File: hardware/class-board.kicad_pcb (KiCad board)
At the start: 4 copper layers, 180 x 100 mm, 334 parts, among them J1 DevKit J1 (left row), J10 C2937625_-_Conn_01x03, J11 C2937625_-_Conn_01x03, J12 C2937625_-_Conn_01x03, J13 C492401-PZ254V-11-02P, J2 DevKit J3 (right row), J201 USB-C 16P, J202 DC005-T20, J3 C2937625_-_Conn_01x03, J4 Qwiic, J5 Expansion 2x10, J6 Panel link 2x20 female, J7 Panel link 2x20 female, J8 Panel link 2x20 female, J9 C2937625_-_Conn_01x03, J901 KF301-5.0-2P, J903 KF301-5.0-2P, J905 KF301-5.0-3P, Q901 AOD4185, Q904 AOD4184A, U101 ADS8688IDBTR, U201 LM66100DCKR, U202 LM66100DCKR, U203 78L05G-AB3-R, U204 AMS1117-3.3, U301 DAC8563SDGSR, U302 74HCT125PW, U303 OPA2192IDR, U501 SN74AHCT541PWR, U502 74HCT125PW, U503 SN74LVC1T45DBVR, U505 TCA9535PWR, U701 SI5351A-B-GT, U702 74HC74D,653, U703 OPA1656IDR, U704 DG419DY-T1-E3, U705 OPA1612AIDR, U706 OPA1612AIDR, U801 AD9834BRUZ, U802 OPA564AIDWPR, U901 TS5A23157DGSR, U902 TS5A23157DGSR, U903 DRV8871DDAR, U904 UCC27517DBVR, Y701 25 MHz

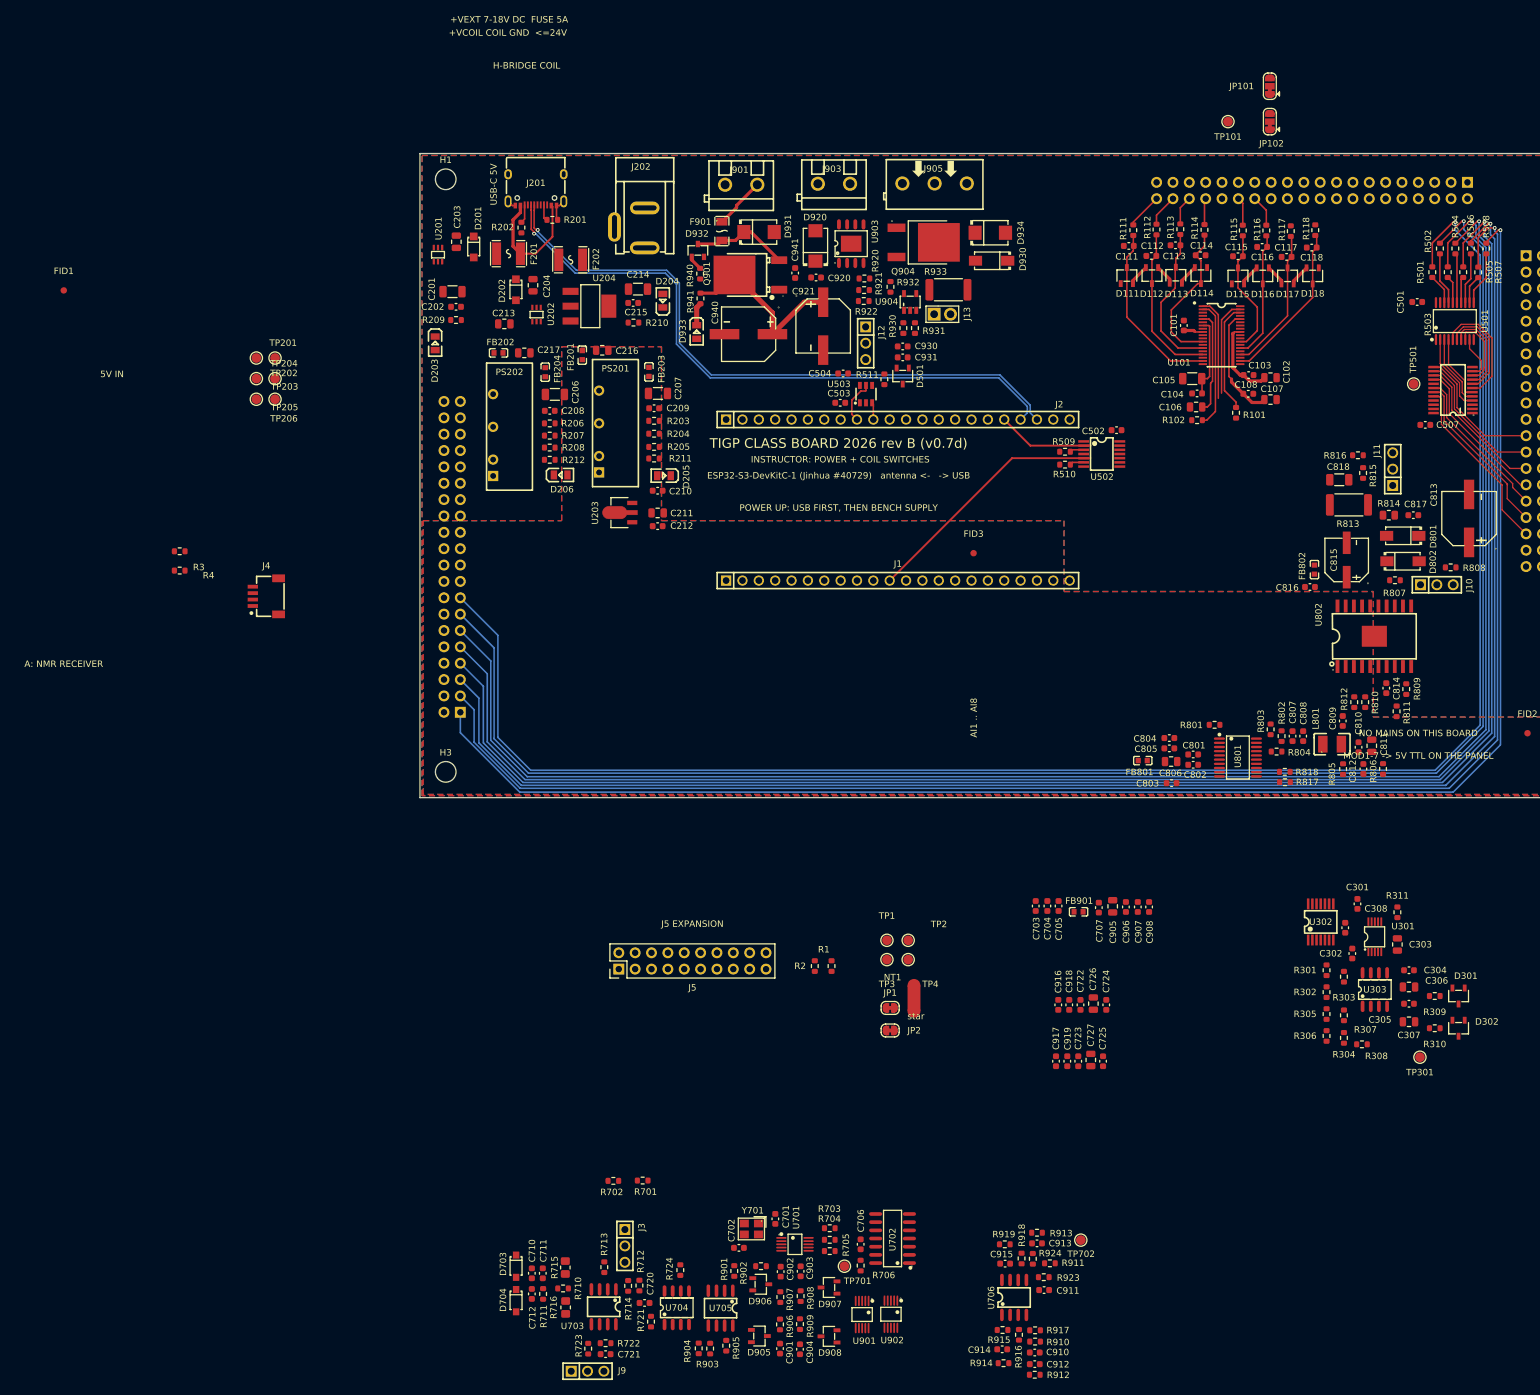
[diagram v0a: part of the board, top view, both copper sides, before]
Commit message: hardware: main-board PCB from the instructor's 2026-09-19 05:05 save (790 tracks, 17 parts still parked)
Co-Authored-By: Claude Fable 5.1 <noreply@anthropic.com>
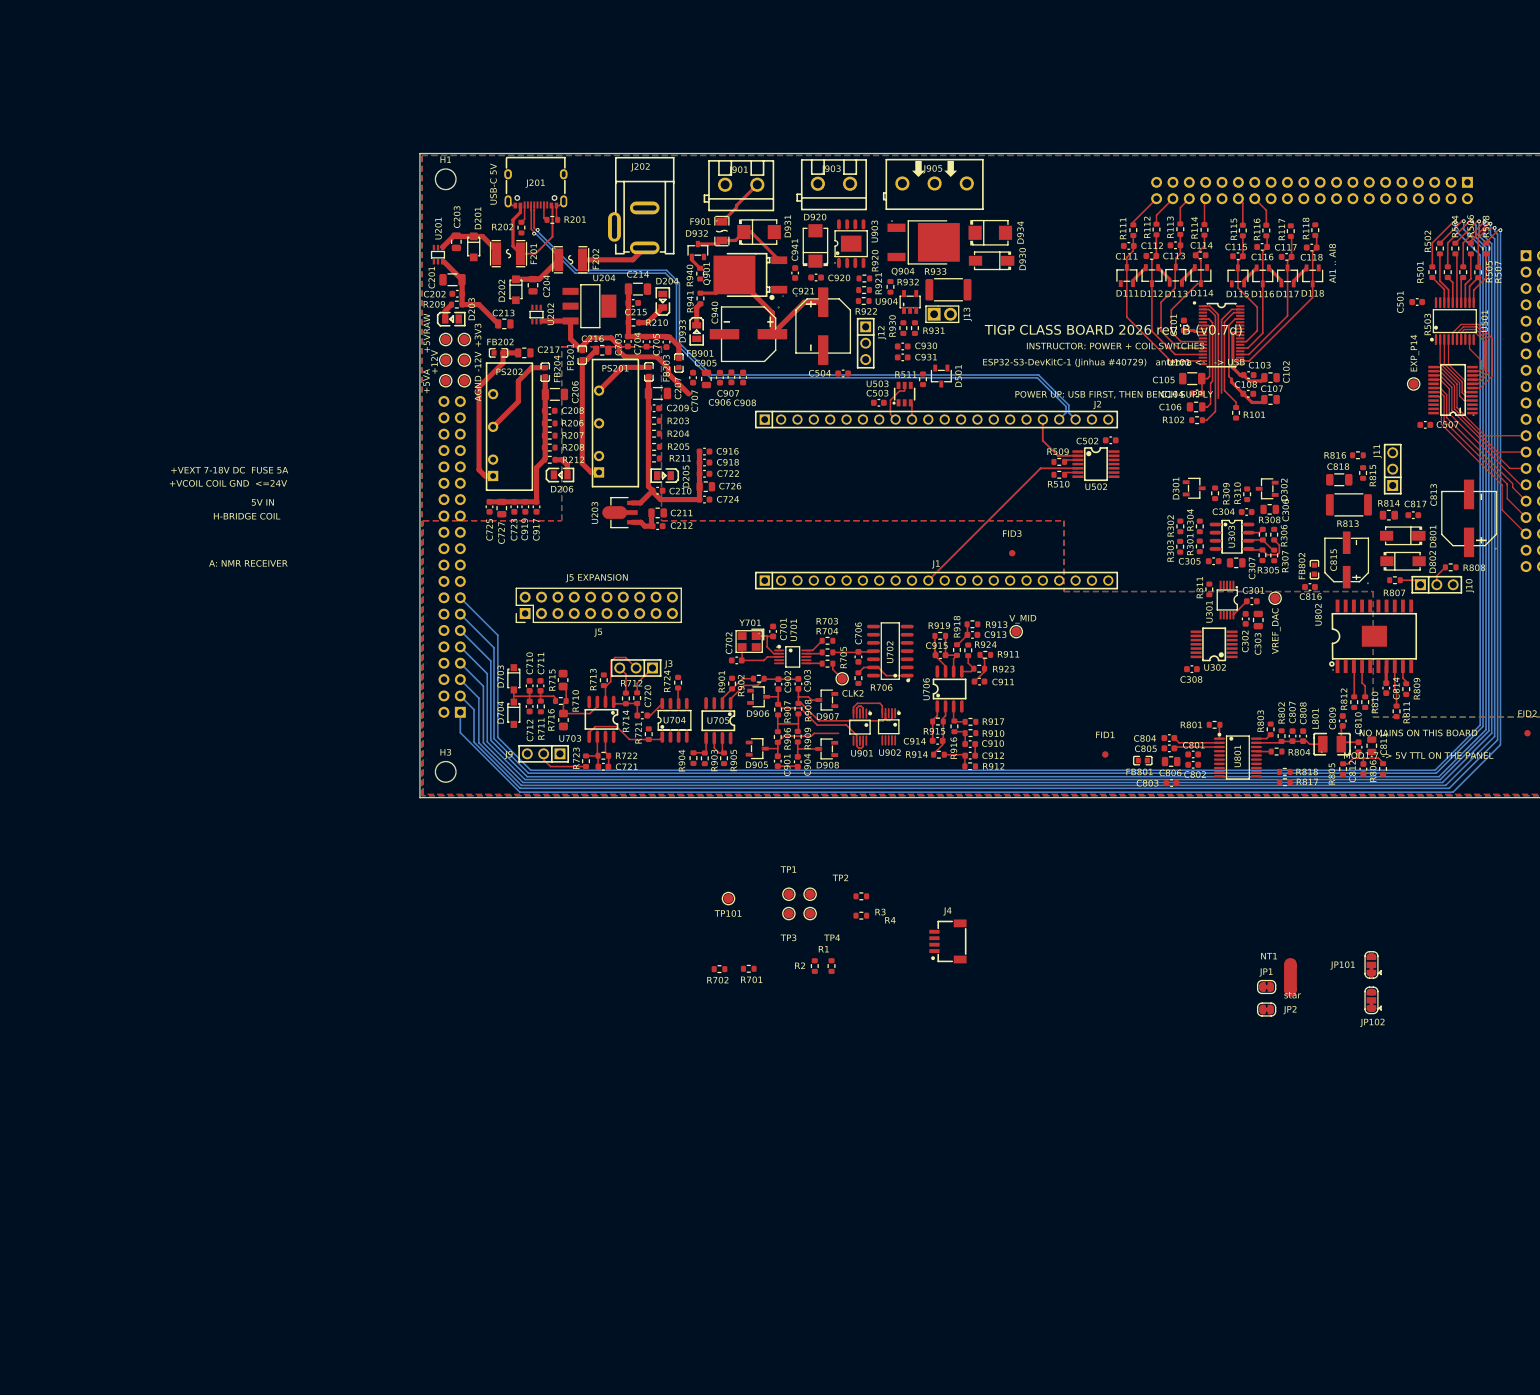
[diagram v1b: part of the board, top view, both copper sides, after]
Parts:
- moved FID1 177.0 mm to (106.4, 108.3)
- moved TP101 143.4 mm to (47.9, 130.7)
- moved JP101 137.3 mm to (147.7, 141.0)
- moved JP102 137.3 mm to (147.7, 146.5)
- moved C725 128.4 mm to (10.8, 69.8), turned to -90 degrees
- moved C727 125.3 mm to (12.7, 70.1), turned to -90 degrees
- moved C723 122.8 mm to (14.7, 69.8), turned to -90 degrees
- moved C919 120.4 mm to (16.4, 69.8), turned to -90 degrees
- moved J4 118.6 mm to (81.9, 137.3)
- moved R3 118.6 mm to (68.5, 130.3)
- moved R4 118.6 mm to (68.5, 133.3)
- moved C917 118.0 mm to (18.1, 69.8), turned to -90 degrees
- moved C703 108.1 mm to (32.3, 44.2)
- moved C704 107.5 mm to (35.2, 44.2), turned to -90 degrees
- moved C705 106.6 mm to (38.3, 44.3), turned to -90 degrees
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- renumbered TP203 to +12V, TP202 to +3V3, TP205 to +5VA, TP201 to +5VRAW, TP204 to -12V, TP206 to AGND, TP701 to CLK2, TP501 to EXP_P14, TP301 to VREF_DAC, TP702 to V_MID
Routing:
- net +5V_RAW: track 0.00 -> 46.8 mm
- net +12V: track 13.2 -> 50.5 mm
- net -12V: track 6.46 -> 33.7 mm
- net Net-(PS202-+VIN): track 0.00 -> 24.6 mm
- net /nmr_rx/SN_B: track 0.00 -> 23.3 mm
- net /nmr_rx/SN_A: track 0.00 -> 22.2 mm
- net Net-(PS201-+VIN): track 0.00 -> 22.1 mm
- net +3V3: track 17.8 -> 38.2 mm
- net /nmr_rx/SP_A: track 0.00 -> 17.0 mm
- net Net-(PS202--VO): track 0.00 -> 13.8 mm
- net /nmr_rx/ST2_IN: track 0.00 -> 13.4 mm
- net /nmr_rx/S_MINUS: track 0.00 -> 12.5 mm
- net /b1_inputs/AUX: track 0.00 -> 12.2 mm
- net /nmr_rx/LNA_FB1: track 0.00 -> 11.9 mm
- net /nmr_rx/RX_IN: track 0.00 -> 11.0 mm
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
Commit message: WIP main board routing + schematic (instructor), 2026-09-21 05:04
Co-Authored-By: Claude Fable 5.1 <noreply@anthropic.com>
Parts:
- removed +12V, +3V3, +5VA, +5VRAW, -12V, AGND, EXP_P14, VREF_DAC: TP, class_board:TestPoint_Pad_D1.5mm
- removed CLK2: CLK2, class_board:TestPoint_Pad_D1.5mm
- removed JP1, JP2: SolderJumper_2_Bridged, class_board:SolderJumper-2_P1.3mm_Bridged_RoundedPad1.0x1.5mm
- removed JP101, JP102: SolderJumper_3_Bridged12, class_board:SolderJumper-3_P1.3mm_Bridged12_RoundedPad1.0x1.5mm
- removed NT1: AGND-GND star, class_board:NetTie-2_SMD_Pad2.0mm
- removed V_MID: V_MID, class_board:TestPoint_Pad_D1.5mm
- added J14: C2937625_-_Conn_01x03, DDS_Library:C2937625-HDR-TH_3P-P2.54-V-M, F.Cu at (136.9, 31.3)
- added J15: C2937625_-_Conn_01x03, DDS_Library:C2937625-HDR-TH_3P-P2.54-V-M, F.Cu at (138.6, 28.0)
- added R717: 0, Resistor_SMD:R_0805_2012Metric_Pad1.20x1.40mm_HandSolder, F.Cu at (11.4, 76.9)
- added R718: 0, Resistor_SMD:R_0805_2012Metric_Pad1.20x1.40mm_HandSolder, F.Cu at (11.3, 79.1)
- added R719: 0, Resistor_SMD:R_0805_2012Metric_Pad1.20x1.40mm_HandSolder, F.Cu at (113.4, 142.4)
- added TP201: 5V_RAW, class_board:TestPoint_Pad_D1.5mm, F.Cu at (8.80, 33.7)
- added TP202: +3V3, class_board:TestPoint_Pad_D1.5mm, F.Cu at (20.8, 36.8)
- added TP203: +12V, class_board:TestPoint_Pad_D1.5mm, F.Cu at (44.1, 56.5)
- added TP204: -12V, class_board:TestPoint_Pad_D1.5mm, F.Cu at (21.1, 69.2)
- added TP205: +5VA, class_board:TestPoint_Pad_D1.5mm, F.Cu at (108.9, 127.7)
- added TP206: AGND, class_board:TestPoint_Pad_D1.5mm, F.Cu at (108.9, 131.2)
- added TP301: VREF, class_board:TestPoint_Pad_D1.5mm, F.Cu at (133.2, 82.8)
- added TP501: EXP_P14, class_board:TestPoint_Pad_D1.5mm, F.Cu at (75.7, 99.0)
- added TP701: CLK2, class_board:TestPoint_Pad_D1.5mm, F.Cu at (65.8, 96.5)
- added TP702: V_MID, class_board:TestPoint_Pad_D1.5mm, F.Cu at (92.5, 106.8)
- R715, R716, R933: value 0 -> 0R
- TP1: value TP -> RST
- TP101: value TP -> AGND
- TP2: value TP -> GND
- TP3: value TP -> +3V3
- TP4: value TP -> +5V
- moved R2 65.7 mm to (94.7, 84.6), turned to -90 degrees
- moved R1 65.2 mm to (96.5, 84.6), turned to -90 degrees
- moved R702 30.1 mm to (72.2, 125.8)
- moved TP2 11.9 mm to (65.3, 119.2)
- moved R118 8.66 mm to (138.0, 35.5)
- moved C118 8.51 mm to (138.2, 38.1)
- moved J4 8.45 mm to (88.3, 131.9)
- moved C117 7.67 mm to (133.2, 38.6)
- moved R117 7.67 mm to (133.9, 34.6)
- moved D117 7.53 mm to (134.4, 41.5)
- moved D118 7.53 mm to (138.3, 41.5)
- moved D802 4.15 mm to (152.5, 74.2)
- moved D801 3.59 mm to (152.1, 77.9), turned to 0 degrees
- moved TP4 2.53 mm to (63.1, 132.8)
- moved R912 1.68 mm to (83.8, 110.2), turned to 0 degrees
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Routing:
- net AGND: track 0.00 -> 162.8 mm, vias 0 -> 87
- net /b5_dio_trig/OPTO_IN1: track 0.00 -> 144.2 mm, vias 0 -> 1
- net /b5_dio_trig/OPTO_IN2: track 0.00 -> 136.4 mm, vias 0 -> 1
- net GND: track 5.01 -> 135.3 mm, vias 0 -> 68
- net /b1_inputs/COND_OUT1: track 5.64 -> 124.3 mm
- net /b1_inputs/COND_OUT2: track 6.22 -> 115.6 mm
- net /base_mcu/DDS_PSEL: track 0.00 -> 108.9 mm, vias 0 -> 1
- net /base_mcu/HB_IN1: track 0.00 -> 97.7 mm, vias 0 -> 2
- net /base_mcu/DDS_FSYNC: track 0.00 -> 94.8 mm, vias 0 -> 1
- net /base_mcu/HB_IN2: track 0.00 -> 92.1 mm, vias 0 -> 2
- net /base_mcu/GPIO44: track 0.00 -> 65.0 mm
- net /base_mcu/TRIG_IO: track 2.68 -> 66.9 mm, vias 0 -> 1
- net /base_mcu/GPIO43: track 0.00 -> 60.5 mm
- net /b1_inputs/AO1: track 0.00 -> 57.4 mm
- net /b1_inputs/AO2: track 0.00 -> 52.9 mm
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- added copper zone on F.Cu, net (none)
- added copper zone on F.Cu, net +VEXT
- added copper zone on B.Cu, net /b1_inputs/TX
- added copper zone on F.Cu, net /c_switch/COIL
- added copper zone on F.Cu, net /c_switch/HB_OUT1
- added copper zone on F.Cu, net /c_switch/HB_OUT2
- added copper zone on F.Cu, net /nmr_tx/+VEXT_TX
- added copper zone on F.Cu, net /nmr_tx/TX_A
- removed copper zone on B.Cu, net GND
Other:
- board text removed: "NO MAINS ON THIS BOARD"
- board text removed: "star"
